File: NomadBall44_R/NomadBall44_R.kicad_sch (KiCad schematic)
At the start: 52 parts, among them SW1 SW_Push, SW10 SW_Push, SW11 SW_Push, SW12 SW_Push, SW13 SW_Push, SW14 SW_Push, SW15 SW_Push, SW16 SW_Push, SW17 SW_Push, SW18 SW_Push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

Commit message: トラックボール基板発注ようにIC部品を割り当て
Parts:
- U1: footprint footprints:XIAO-nRF52840-Plus-Hole-SMD -> footprints:XIAO-nRF52840-Plus-Through-Hole
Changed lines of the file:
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@@
 			)
 		)
-		(property "Footprint" "footprints:XIAO-nRF52840-Plus-Hole-SMD"
+		(property "Footprint" "footprints:XIAO-nRF52840-Plus-Through-Hole"
 			(at 57.658 50.8 0)
 			(effects

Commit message: ロータリエンコーダーのフットプリントを割り当て
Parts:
- SW26: footprint (none) -> Rotary_Encoder:RotaryEncoder_Alps_EC12E-Switch_Vertical_H20mm
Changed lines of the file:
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@@
 			)
 		)
-		(property "Footprint" ""
+		(property "Footprint" "Rotary_Encoder:RotaryEncoder_Alps_EC12E-Switch_Vertical_H20mm"
 			(at 138.43 107.696 0)
 			(effects

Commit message: NomadBall44用のシンボルライブラリを作成
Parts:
- removed J1: ~, myfootprintLibrary:pmw3610_connector, symbol roba:pmw3610_breakout
- removed U1: XIAO-nRF52840-Plus-SMD, footprints:XIAO-nRF52840-Plus-Through-Hole, symbol Seeed_Studio_XIAO_Series:XIAO-nRF52840_Plus_SMD
- added J1: ~, myfootprintLibrary:pmw3610_connector, symbol NomadBall44:pmw3610_breakout
- added U1: XIAO-nRF52840-Plus-SMD, footprints:XIAO-nRF52840-Plus, symbol NomadBall44:XIAO-nRF52840_Plus_SMD
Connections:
- net 3.3V: now also J1.4 (Vin), U1.12 (3V3)
- net Bat: now also U1.32 (VBAT)
- net CS: now also J1.2 (nCS), U1.3 (P0.28_A2_D2)
- net Col0: now also U1.15 (P0.15_D11_I2S_SD)
- net Col1: now also U1.16 (P0.19_D12_I2S_SCK)
- net Col2: now also U1.17 (P1.01_D13_I2S_WS)
- net Col3: now also U1.18 (P0.09_D14_NFC1_RX1)
- net Col4: now also U1.19 (P0.10_D15_NFC2_TX1)
- net Col5: now also U1.21 (P1.03_D17_SCK1)
- net GND: now also J1.3 (GND), U1.13 (GND), U1.33 (GND)
- net MOTION: now also J1.7 (MOTION), U1.4 (P0.29_A3_D3)
- net RE_A: now also U1.5 (P0.04_A4_D4_SDA)
- net RE_B: now also U1.6 (P0.05_A5_D5_SCL)
- net Row0: now also U1.11 (P1.15_D10_MOSI)
- net Row1: now also U1.10 (P1.14_D9_MISO)
- net Row2: now also U1.8 (P1.12_D7_RX), U1.9 (P1.13_D8_SCK)
- net SCLK: now also J1.1 (SCLK), U1.2 (P0.03_A1_D1)
- net SDIO: now also J1.6 (SDIO), U1.1 (P0.02_A0_D0)
- net VCC: now also U1.14 (VBUS)

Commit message: pmw3610のコネクター用フットプリントを追加
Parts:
- J1: footprint myfootprintLibrary:pmw3610_connector -> footprints:pmw3610_connector
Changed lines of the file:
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@@
 			)
 		)
-		(property "Footprint" "myfootprintLibrary:pmw3610_connector"
+		(property "Footprint" "footprints:pmw3610_connector"
 			(at 72.39 110.49 0)
 			(effects

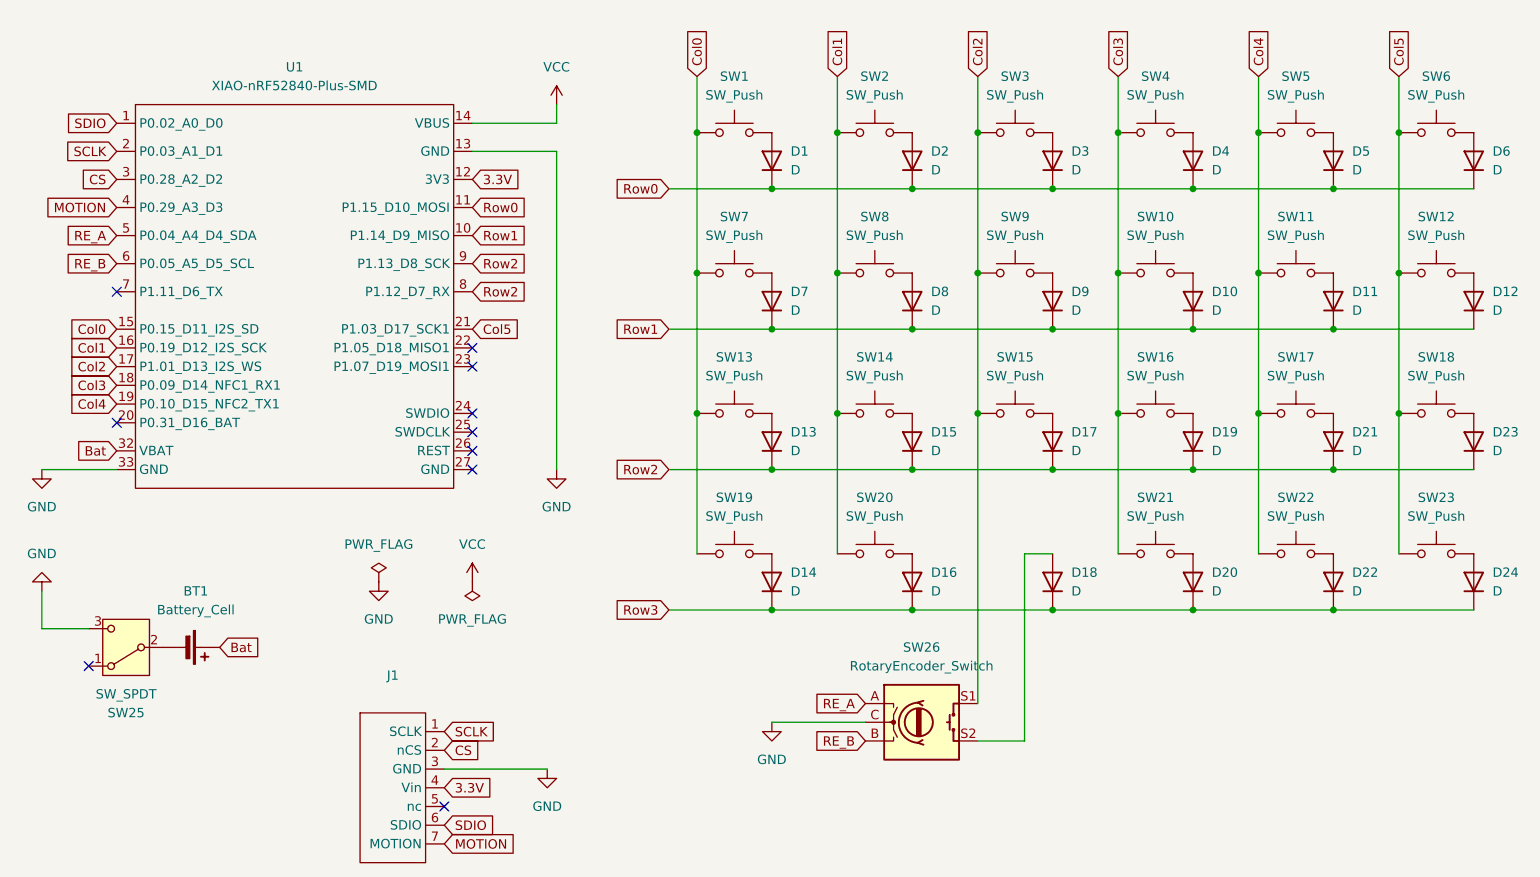
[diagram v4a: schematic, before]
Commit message: シンボルとフットプリントのライブラリのパスを修正
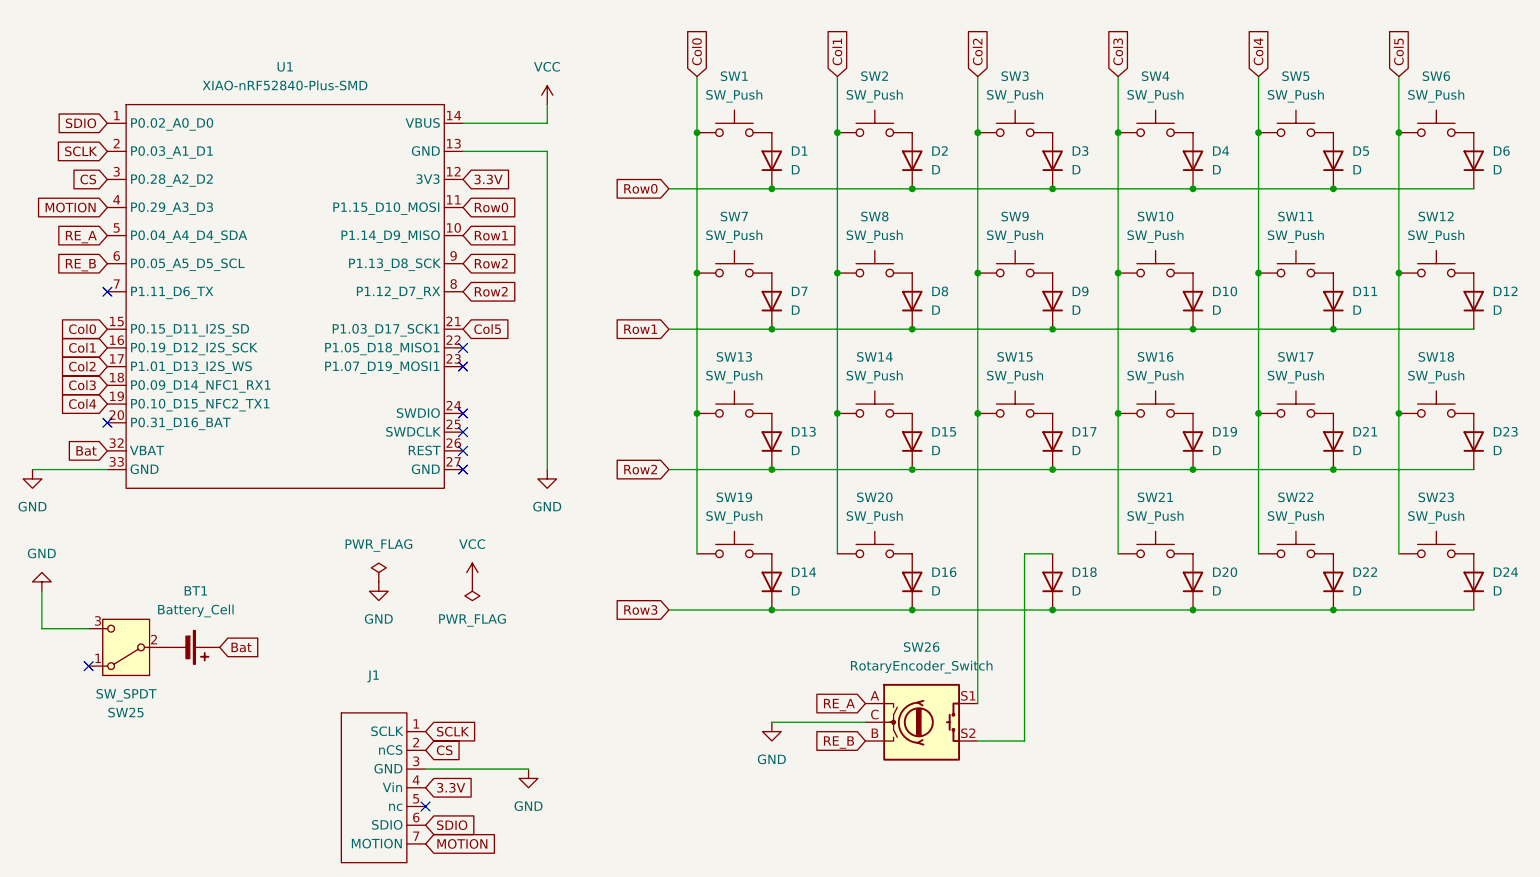
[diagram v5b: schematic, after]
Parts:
- J1: footprint footprints:pmw3610_connector -> NomadBall44:pmw3610_connector
- U1: footprint footprints:XIAO-nRF52840-Plus -> NomadBall44:XIAO-nRF52840-Plus

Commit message: キースイッチのシンボルにフットプリントを割り当て
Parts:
- BT1: footprint (none) -> NomadBall44:JST_S2B-PH-SM4-TB
- D1, D10, D11, D12, D13, D2, D24, D3, D4, D5, D6, D7, D8, D9: footprint (none) -> NomadBall44:Diode_SMD
- D14: renamed from D15; footprint (none) -> NomadBall44:Diode_SMD
- D15: renamed from D17; footprint (none) -> NomadBall44:Diode_SMD
- D16: renamed from D19; footprint (none) -> NomadBall44:Diode_SMD
- D17: renamed from D21; footprint (none) -> NomadBall44:Diode_SMD
- D18: renamed from D23; footprint (none) -> NomadBall44:Diode_SMD
- D19: renamed from D14; footprint (none) -> NomadBall44:Diode_SMD
- D20: renamed from D16; footprint (none) -> NomadBall44:Diode_SMD
- D21: renamed from D18; footprint (none) -> NomadBall44:Diode_SMD
- D22: renamed from D20; footprint (none) -> NomadBall44:Diode_SMD
- D23: renamed from D22; footprint (none) -> NomadBall44:Diode_SMD
- SW1, SW10, SW11, SW12, SW13, SW14, SW15, SW16, SW17, SW18, SW2, SW25, SW3, SW4, SW5, SW6, SW7, SW8, SW9: footprint (none) -> NomadBall44:Choc_v2_Hotswap_1u
- SW19, SW20: footprint (none) -> NomadBall44:Kailh_Choc_V1_Hotswap_thin_via
- SW22: renamed from SW21; footprint (none) -> NomadBall44:Choc_v2_Hotswap_1u
- SW23: renamed from SW22; footprint (none) -> NomadBall44:Choc_v2_Hotswap_1u
- SW24: renamed from SW23; footprint (none) -> NomadBall44:Choc_v2_Hotswap_1u
- renumbered SW26 to SW21

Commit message: 水平スライドスイッチのフットプリントを追加
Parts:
- SW25: footprint NomadBall44:Choc_v2_Hotswap_1u -> NomadBall44:TGSW_MSK-12D19
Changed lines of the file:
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@@
 			)
 		)
-		(property "Footprint" "NomadBall44:Choc_v2_Hotswap_1u"
+		(property "Footprint" "NomadBall44:TGSW_MSK-12D19"
 			(at 34.29 101.6 0)
 			(effects

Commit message: デバッグするためにリファレンスフィールドを表示するようにした
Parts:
- removed D23, D24: D, NomadBall44:Diode_SMD, symbol Device:D
- removed SW23, SW24: SW_Push, NomadBall44:Choc_v2_Hotswap_1u, symbol Switch:SW_Push
- renumbered SW25 to SW23
